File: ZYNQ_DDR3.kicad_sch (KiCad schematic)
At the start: 69 parts, among them U24 TPS51200DRC, U25 MT41J256M16, U8 XC7Z020-CLG484

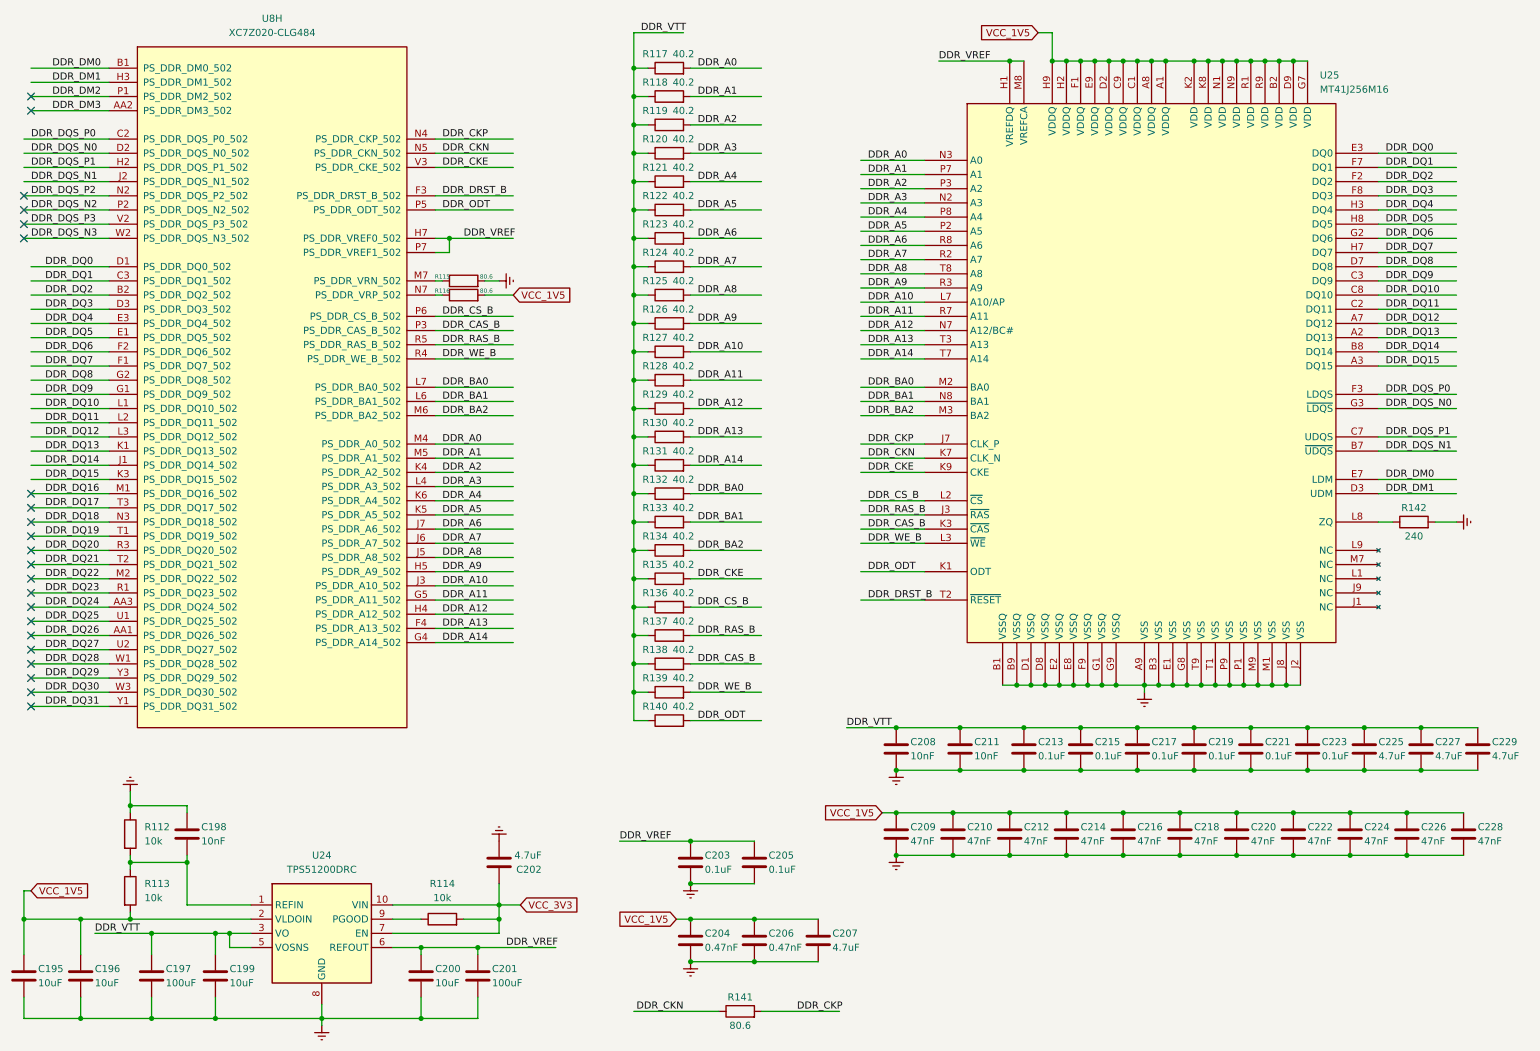
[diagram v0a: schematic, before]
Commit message: 变压器输入+两块DDR3
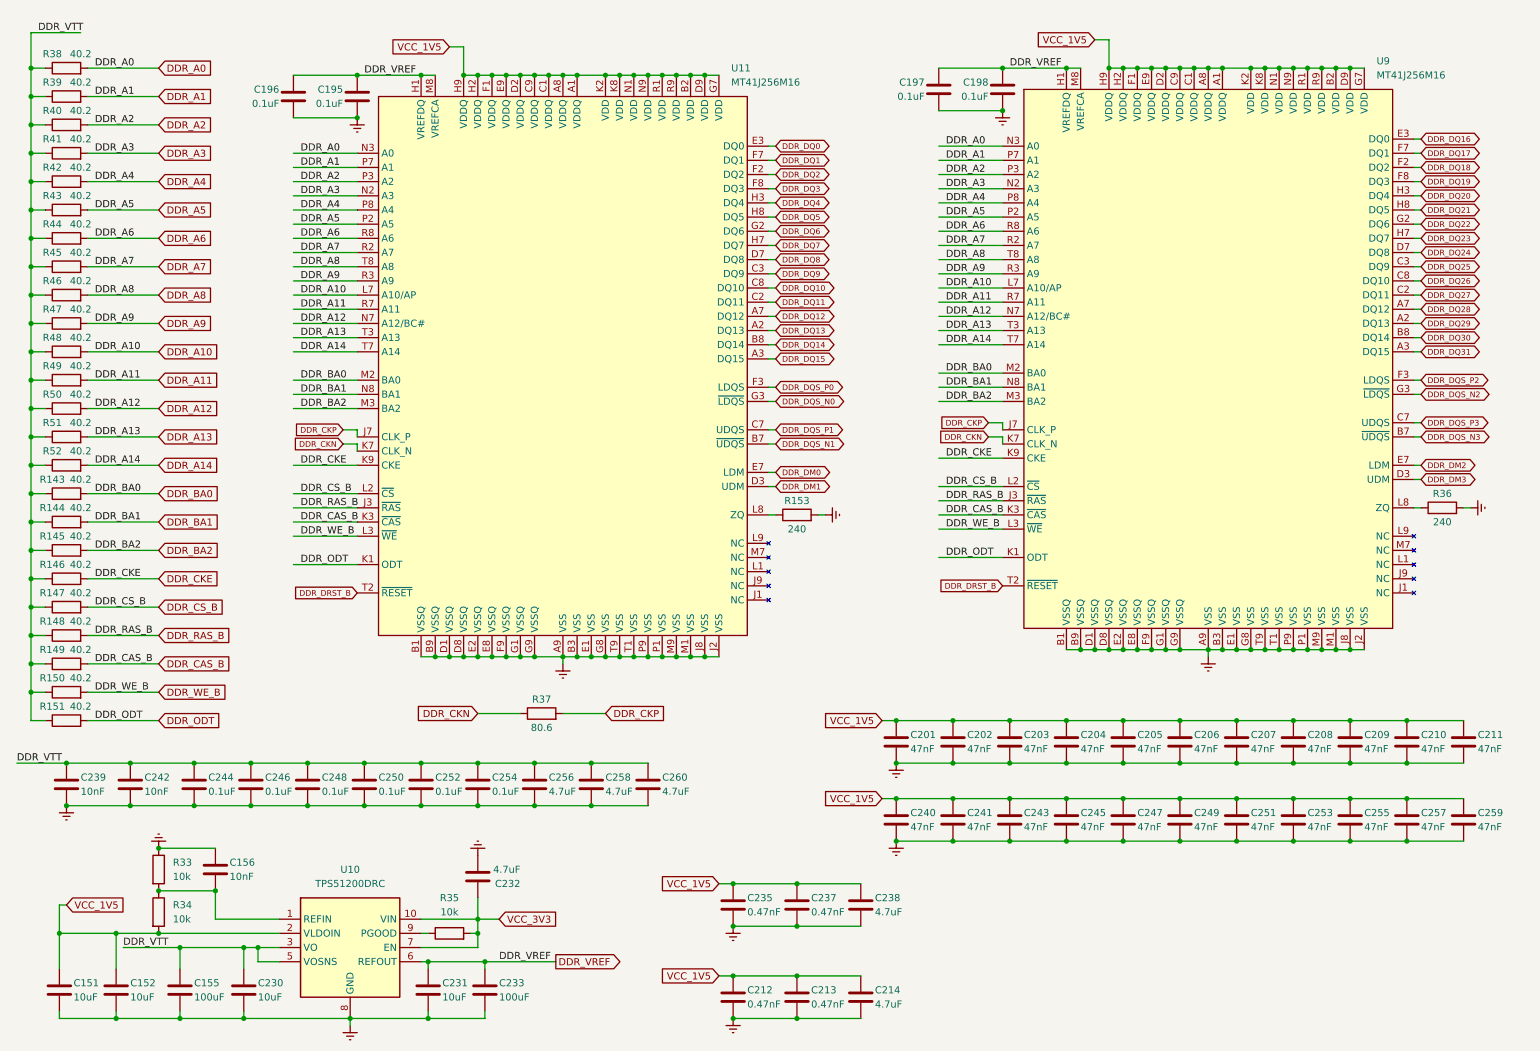
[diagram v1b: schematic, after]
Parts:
- removed R115, R116, R141: 80.6, Resistor_SMD:R_0402_1005Metric, symbol Device:R
- removed U8: XC7Z020-CLG484, Package_BGA:Xilinx_CLG484_CLG485, symbol Zynq7020_AD9238:XC7Z020-CLG484
- added C195, C196, C197, C198: 0.1uF, Capacitor_SMD:C_0402_1005Metric, symbol Device:C
- added C201, C202, C204, C206, C207, C208, C209, C210, C211: 47nF, Capacitor_SMD:C_0402_1005Metric, symbol Device:C
- added C212, C213: 0.47nF, Capacitor_SMD:C_0402_1005Metric, symbol Device:C
- added C214: 4.7uF, Capacitor_SMD:C_0603_1608Metric, symbol Device:C
- added R36: 240, Resistor_SMD:R_0402_1005Metric, symbol Device:R
- added R37: 80.6, Resistor_SMD:R_0402_1005Metric, symbol Device:R
- added U9: MT41J256M16, Package_BGA:Micron_FBGA-96_9x14mm_Layout9x16_P0.8mm, symbol Zynq7020_AD9238:MT41J256M16
- C203, C205: value 0.1uF -> 47nF
- renumbered C195 to C151, C196 to C152, C197 to C155, C198 to C156, C199 to C230, C200 to C231, C202 to C232, C201 to C233, C204 to C235, C206 to C237, C207 to C238, C208 to C239, C209 to C240, C210 to C241, C211 to C242, C212 to C243, C213 to C244, C214 to C245, C215 to C246, C216 to C247, C217 to C248, C218 to C249, C219 to C250, C220 to C251, C221 to C252, C222 to C253, C223 to C254, C224 to C255, C225 to C256, C226 to C257, C227 to C258, C228 to C259, C229 to C260, R132 to R143, R133 to R144, R134 to R145, R135 to R146, R136 to R147, R137 to R148, R138 to R149, R139 to R150, R140 to R151, R142 to R153, R112 to R33, R113 to R34, R114 to R35, R117 to R38, R118 to R39, R119 to R40, R120 to R41, R121 to R42, R122 to R43, R123 to R44, R124 to R45, R125 to R46, R126 to R47, R127 to R48, R128 to R49, R129 to R50, R130 to R51, R131 to R52, U24 to U10, U25 to U11
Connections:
- net DDR_A0: now also U9.N3 (A0)
- net DDR_A1: now also U9.P7 (A1)
- net DDR_A10: now also U9.L7 (A10/AP)
- net DDR_A11: now also U9.R7 (A11)
- net DDR_A12: now also U9.N7 (A12/BC#)
- net DDR_A13: now also U9.T3 (A13)
- net DDR_A14: now also U9.T7 (A14)
- net DDR_A2: now also U9.P3 (A2)
- net DDR_A3: now also U9.N2 (A3)
- net DDR_A4: now also U9.P8 (A4)
- net DDR_A5: now also U9.P2 (A5)
- net DDR_A6: now also U9.R8 (A6)
- net DDR_A7: now also U9.R2 (A7)
- net DDR_A8: now also U9.T8 (A8)
- net DDR_A9: now also U9.R3 (A9)
- net DDR_BA0: now also U9.M2 (BA0)
- net DDR_BA1: now also U9.N8 (BA1)
- net DDR_BA2: now also U9.M3 (BA2)
- net DDR_CAS_B: now also U9.K3 (~{CAS})
- net DDR_CKE: now also U9.K9 (CKE)
- net DDR_CKN: now also R37.1, U9.K7 (CLK_N)
- net DDR_CKP: now also R37.2, U9.J7 (CLK_P)
- net DDR_CS_B: now also U9.L2 (~{CS})
- net DDR_DM2: now also U9.E7 (LDM)
- net DDR_DM3: now also U9.D3 (UDM)
- net DDR_DQ16: now also U9.E3 (DQ0)
- net DDR_DQ17: now also U9.F7 (DQ1)
- net DDR_DQ18: now also U9.F2 (DQ2)
- net DDR_DQ19: now also U9.F8 (DQ3)
- net DDR_DQ20: now also U9.H3 (DQ4)
- net DDR_DQ21: now also U9.H8 (DQ5)
- net DDR_DQ22: now also U9.G2 (DQ6)
- net DDR_DQ23: now also U9.H7 (DQ7)
- net DDR_DQ24: now also U9.D7 (DQ8)
- net DDR_DQ25: now also U9.C3 (DQ9)
- net DDR_DQ26: now also U9.C8 (DQ10)
- net DDR_DQ27: now also U9.C2 (DQ11)
- net DDR_DQ28: now also U9.A7 (DQ12)
- net DDR_DQ29: now also U9.A2 (DQ13)
- net DDR_DQ30: now also U9.B8 (DQ14)
- net DDR_DQ31: now also U9.A3 (DQ15)
- net DDR_DQS_N2: now also U9.G3 (~{LDQS})
- net DDR_DQS_N3: now also U9.B7 (~{UDQS})
- net DDR_DQS_P2: now also U9.F3 (LDQS)
- net DDR_DQS_P3: now also U9.C7 (UDQS)
- net DDR_DRST_B: now also U9.T2 (~{RESET})
- net DDR_ODT: now also U9.K1 (ODT)
- net DDR_RAS_B: now also U9.J3 (~{RAS})
- net DDR_VREF: now also C195.2, C196.2, C197.2, C198.2, U9.H1 (VREFDQ), U9.M8 (VREFCA); no longer C203.2, C205.2
- net DDR_WE_B: now also U9.L3 (~{WE})
- net Earth: now also C195.1, C196.1, C197.1, C198.1, C201.1, C202.1, C204.1, C206.1, C207.1, C208.1, C209.1, C210.1, C211.1, C212.1, C213.1, C214.1, R36.2, U9.A9 (VSS), U9.B1 (VSSQ), U9.B3 (VSS), U9.B9 (VSSQ), U9.D1 (VSSQ), U9.D8 (VSSQ), U9.E1 (VSS), U9.E2 (VSSQ), U9.E8 (VSSQ), U9.F9 (VSSQ), U9.G1 (VSSQ), U9.G8 (VSS), U9.G9 (VSSQ), U9.J2 (VSS), U9.J8 (VSS), U9.M1 (VSS), U9.M9 (VSS), U9.P1 (VSS), U9.P9 (VSS), U9.T1 (VSS), U9.T9 (VSS)
- net VCC_1V5: now also C203.2, C205.2, C201.2, C202.2, C204.2, C206.2, C207.2, C208.2, C209.2, C210.2, C211.2, C212.2, C213.2, C214.2, U9.A1 (VDDQ), U9.A8 (VDDQ), U9.B2 (VDD), U9.C1 (VDDQ), U9.C9 (VDDQ), U9.D2 (VDDQ), U9.D9 (VDD), U9.E9 (VDDQ), U9.F1 (VDDQ), U9.G7 (VDD), U9.H2 (VDDQ), U9.H9 (VDDQ), U9.K2 (VDD), U9.K8 (VDD), U9.N1 (VDD), U9.N9 (VDD), U9.R1 (VDD), U9.R9 (VDD)
- new net: R36.1, U9.L8 (ZQ)
- no-connect marks 22 -> 0
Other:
- moved on the sheet: C151, C152, C155, C156, C230, C231, C232, C233, C235, C237, C238, C239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

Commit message: 删除-5V电源，添加eMMC模块接口
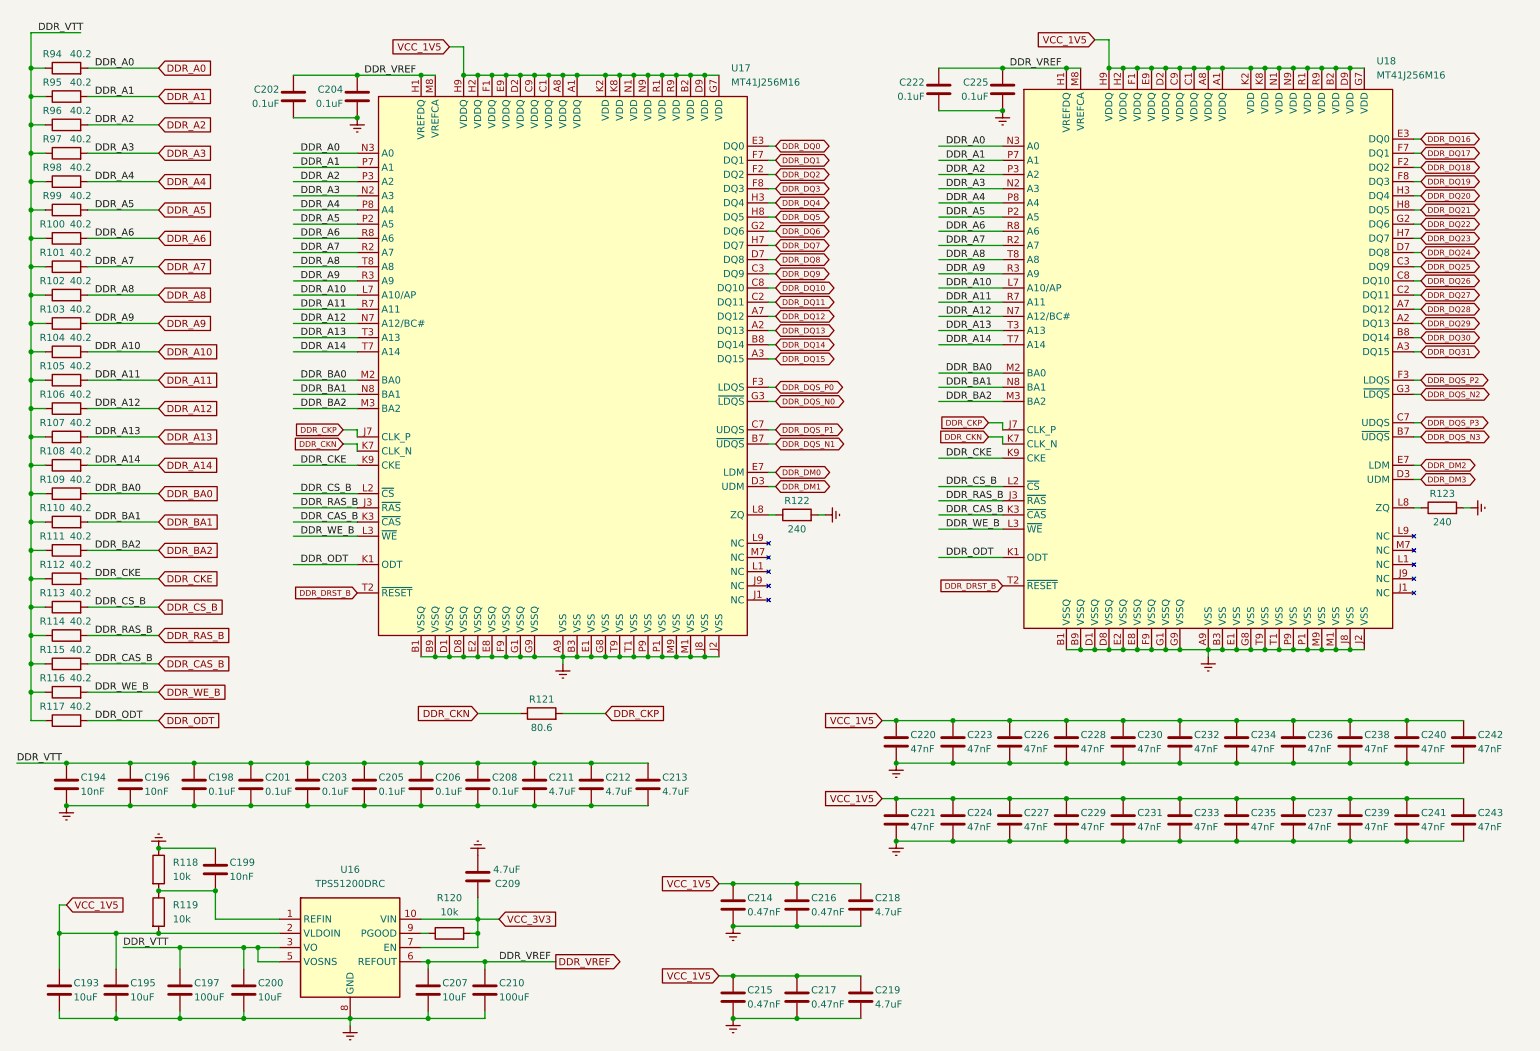
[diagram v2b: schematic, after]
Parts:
- renumbered C151 to C193, C239 to C194, C152 to C195, C242 to C196, C155 to C197, C244 to C198, C156 to C199, C230 to C200, C246 to C201, C196 to C202, C248 to C203, C195 to C204, C250 to C205, C252 to C206, C231 to C207, C254 to C208, C232 to C209, C233 to C210, C256 to C211, C258 to C212, C260 to C213, C235 to C214, C212 to C215, C237 to C216, C213 to C217, C238 to C218, C214 to C219, C201 to C220, C240 to C221, C197 to C222, C202 to C223, C241 to C224, C198 to C225, C203 to C226, C243 to C227, C204 to C228, C245 to C229, C205 to C230, C247 to C231, C206 to C232, C249 to C233, C207 to C234, C251 to C235, C208 to C236, C253 to C237, C209 to C238, C255 to C239, C210 to C240, C257 to C241, C211 to C242, C259 to C243, R44 to R100, R45 to R101, R46 to R102, R47 to R103, R48 to R104, R49 to R105, R50 to R106, R51 to R107, R52 to R108, R143 to R109, R144 to R110, R145 to R111, R146 to R112, R147 to R113, R148 to R114, R149 to R115, R150 to R116, R151 to R117, R33 to R118, R34 to R119, R35 to R120, R37 to R121, R153 to R122, R36 to R123, R38 to R94, R39 to R95, R40 to R96, R41 to R97, R42 to R98, R43 to R99, U10 to U16, U11 to U17, U9 to U18
